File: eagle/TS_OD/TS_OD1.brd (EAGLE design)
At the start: 93.7 x 71.1 mm, 44 parts, among them IC1 LM4558N, T1 2SC1815, T2 2SC1814

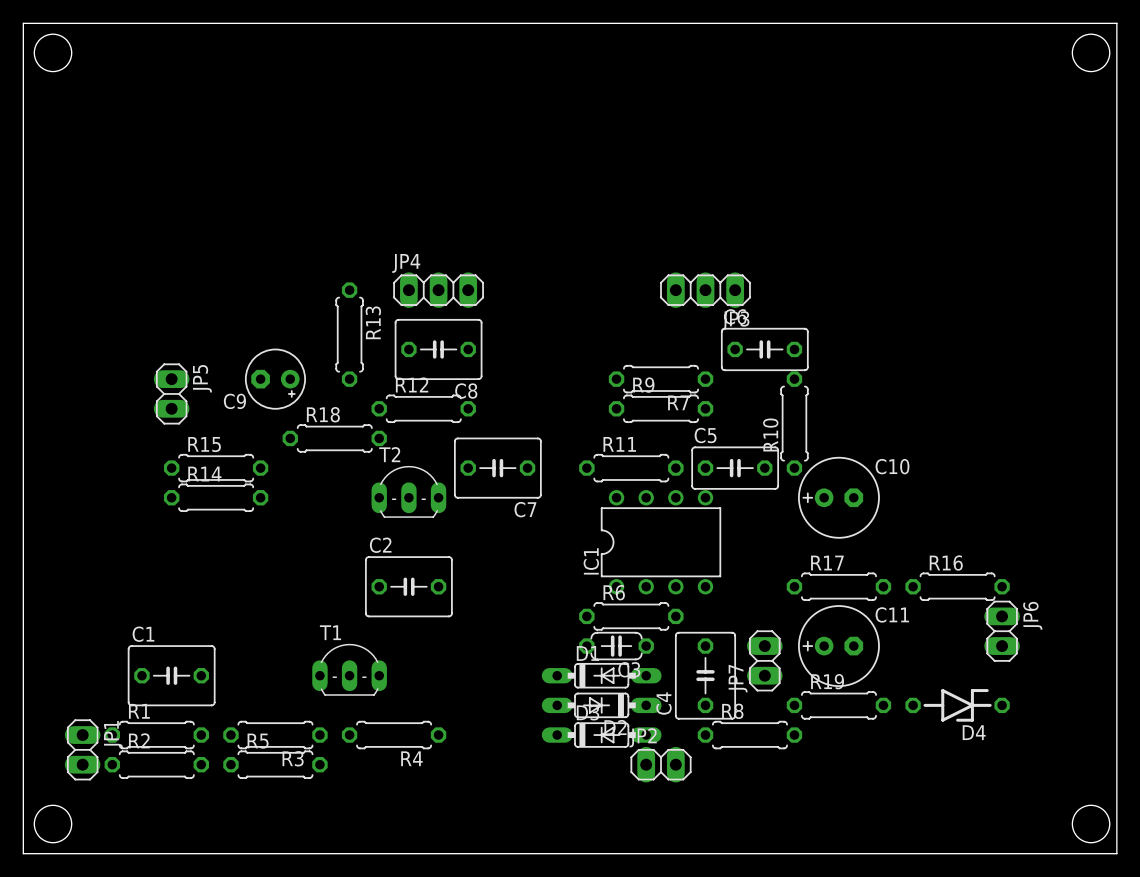
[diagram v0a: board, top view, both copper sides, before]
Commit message: change eagle files' name from TS_OD to TS_OD1
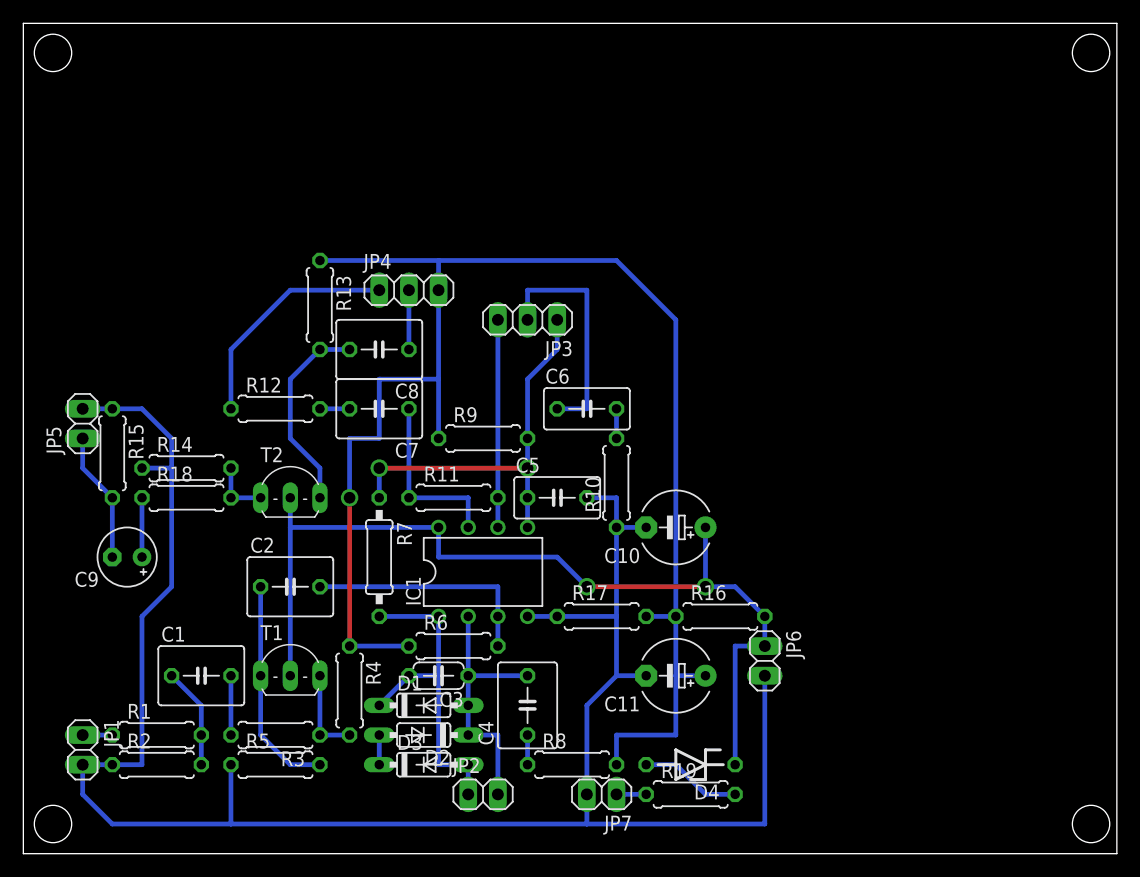
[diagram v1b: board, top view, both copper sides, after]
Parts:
- C10, C11: device rcl:E2,5-7 -> rcl:E5-6
- R7: device rcl:0207/7 -> rcl:0207/10
- moved R7 28.5 mm to (30.5, 25.4), turned to 270 degrees
- moved D4 23.4 mm to (57.1, 7.62)
- moved R16 20.5 mm to (59.7, 20.3)
- moved JP6 20.5 mm to (63.5, 16.5)
- moved R17 20.5 mm to (49.5, 20.3)
- moved C9 19.8 mm to (8.89, 25.4)
- moved JP7 18.1 mm to (49.5, 5.08), turned to 180 degrees
- moved R10 16.1 mm to (50.8, 31.8)
- moved C6 16.1 mm to (48.3, 38.1)
- moved C4 15.5 mm to (43.2, 12.7)
- moved C5 15.5 mm to (45.7, 30.5)
- moved D1 15.5 mm to (34.3, 12.7)
- moved IC1 15.5 mm to (39.4, 24.1)
- moved R11 15.5 mm to (36.8, 30.5)
- moved D2 15.5 mm to (34.3, 10.2)
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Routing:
- net GND: track 0.00 -> 169.3 mm
- net VCC/2: track 0.00 -> 131.6 mm, vias 0 -> 1
- net VCC: track 0.00 -> 80.8 mm, vias 0 -> 2
- net N$4: track 0.00 -> 34.1 mm, vias 0 -> 2
- net N$10: track 0.00 -> 29.0 mm
- net N$8: track 0.00 -> 22.9 mm
- net N$7: track 0.00 -> 20.3 mm
- net N$14: track 0.00 -> 20.3 mm
- net N$17: track 0.00 -> 19.9 mm
- net N$6: track 0.00 -> 18.8 mm
- net N$12: track 0.00 -> 17.8 mm
- net N$19: track 0.00 -> 17.3 mm
- net N$15: track 0.00 -> 15.2 mm
- net N$21: track 0.00 -> 11.2 mm
- net N$2: track 0.00 -> 8.67 mm
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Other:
- board text added: "CutOff"

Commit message: Update: eagle files Add: drawing of the case
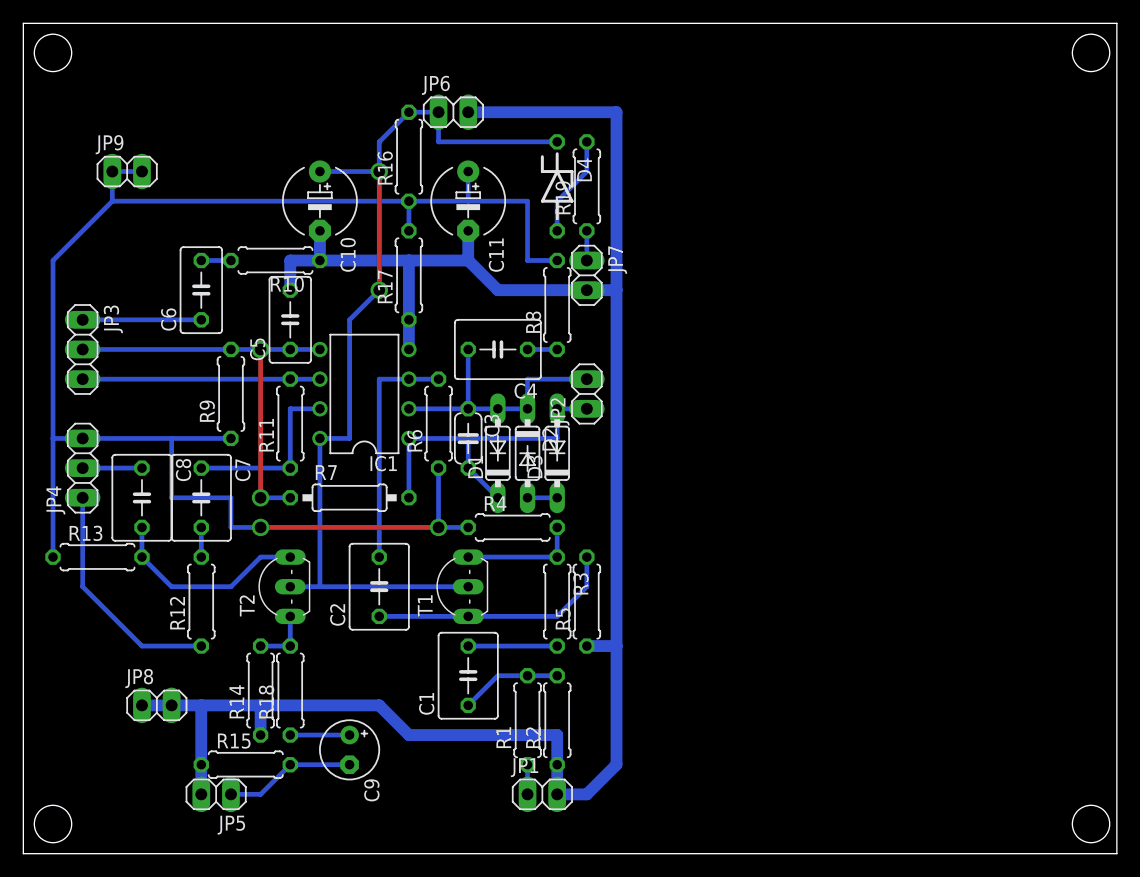
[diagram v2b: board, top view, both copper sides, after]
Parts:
- added JP8: GND, pinhead:1X02
- added JP9: VGND, pinhead:1X02
- C3: value 47pF -> 68pF
- T2: value 2SC1814 -> 2SC1815
- moved JP6 54.0 mm to (36.8, 63.5), turned to 0 degrees
- moved R19 52.8 mm to (48.3, 57.1), turned to 90 degrees
- moved D4 50.8 mm to (45.7, 57.1), turned to 270 degrees
- moved R16 47.6 mm to (33.0, 59.7), turned to 90 degrees
- moved JP7 44.5 mm to (48.3, 49.5), turned to 270 degrees
- moved C11 44.4 mm to (38.1, 55.9), turned to 270 degrees
- moved C10 41.3 mm to (25.4, 55.9), turned to 270 degrees
- moved JP1 39.6 mm to (44.5, 5.08), turned to 0 degrees
- moved R8 39.4 mm to (45.7, 47.0), turned to 90 degrees
- moved JP3 38.2 mm to (5.08, 43.2), turned to 270 degrees
- moved JP2 35.4 mm to (48.3, 39.4), turned to 90 degrees
- moved R10 34.9 mm to (21.6, 50.8), turned to 180 degrees
- moved C6 34.5 mm to (15.2, 48.3), turned to 90 degrees
- moved R2 34.5 mm to (45.7, 11.4), turned to 90 degrees
- moved JP5 33.7 mm to (16.5, 5.08), turned to 180 degrees
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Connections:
- net GND: now also JP8.1, JP8.2
- net N$14: now also JP3.1; no longer JP3.2
- net N$4: now also JP3.2; no longer JP3.1
- net VCC/2: now also JP9.1, JP9.2
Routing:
- net N$14: track 20.3 -> 10.2 mm
- net VCC/2: track 131.6 -> 139.3 mm, vias 1 -> 2
- net GND: track 169.3 -> 173.3 mm
- net N$12: track 17.8 -> 20.3 mm
- net N$6: track 18.8 -> 21.4 mm
- net N$5: track 7.62 -> 10.2 mm
- net N$3: track 5.08 -> 7.62 mm
- net N$4: track 34.1 -> 35.6 mm
